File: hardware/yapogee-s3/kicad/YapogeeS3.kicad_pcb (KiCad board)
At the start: 2 copper layers, 0 parts

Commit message: pick bare s3 parts
Add the daughterboard BOM and checked local symbols and footprints for the bare ESP32-S3R8, high-side RFFC5072A converter, driver and power interfaces. Keep sourcing and review notes private; circuit capture and RF qualification remain.
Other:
- copper layers 2 -> 4
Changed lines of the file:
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@@
 	(title_block
 		(title "Yapogee S3")
-		(date "2026-10-27")
+		(date "2026-10-28")
 		(rev "Draft")
-		(comment 1 "Starter board - outline, stackup and routing not defined")
+		(comment 1 "Four-layer basis; outline, fabrication stackup and routing not defined")
 	)
 	(layers
 		(0 "F.Cu" signal)
+		(4 "In1.Cu" signal)
+		(6 "In2.Cu" signal)
 		(2 "B.Cu" signal)
 		(9 "F.Adhes" user "F.Adhesive")

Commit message: add standalone power and castellated interface
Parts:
- added J100: PCB edge interface, YapogeeS3_ModuleEdge_53x40_Castellated16_P2.00_EM3_v0.2, F.Cu at (100.0, 100.0)
- added J301: USB4105-GF-A-060, USB_C_Receptacle_GCT_USB4105_GF_A_16P, F.Cu at (103.7, 121.0)
- added J501: SMA-J-P-H-ST-EM3, Samtec_SMA_J_P_H_ST_EM3_DropInEdge, F.Cu at (100.0, 133.0)
- added SH1: BMI-S-206-F, KiCad_RF_Shielding_Laird_Technologies_BMI-S-206-F_36.83x33.68mm, F.Cu at (133.2, 120.0)
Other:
- board outline added: 53 x 40 mm
- board text added: "MECHANICAL DRAFT: 53 x 40 mm No circuit placement, nets or routing"

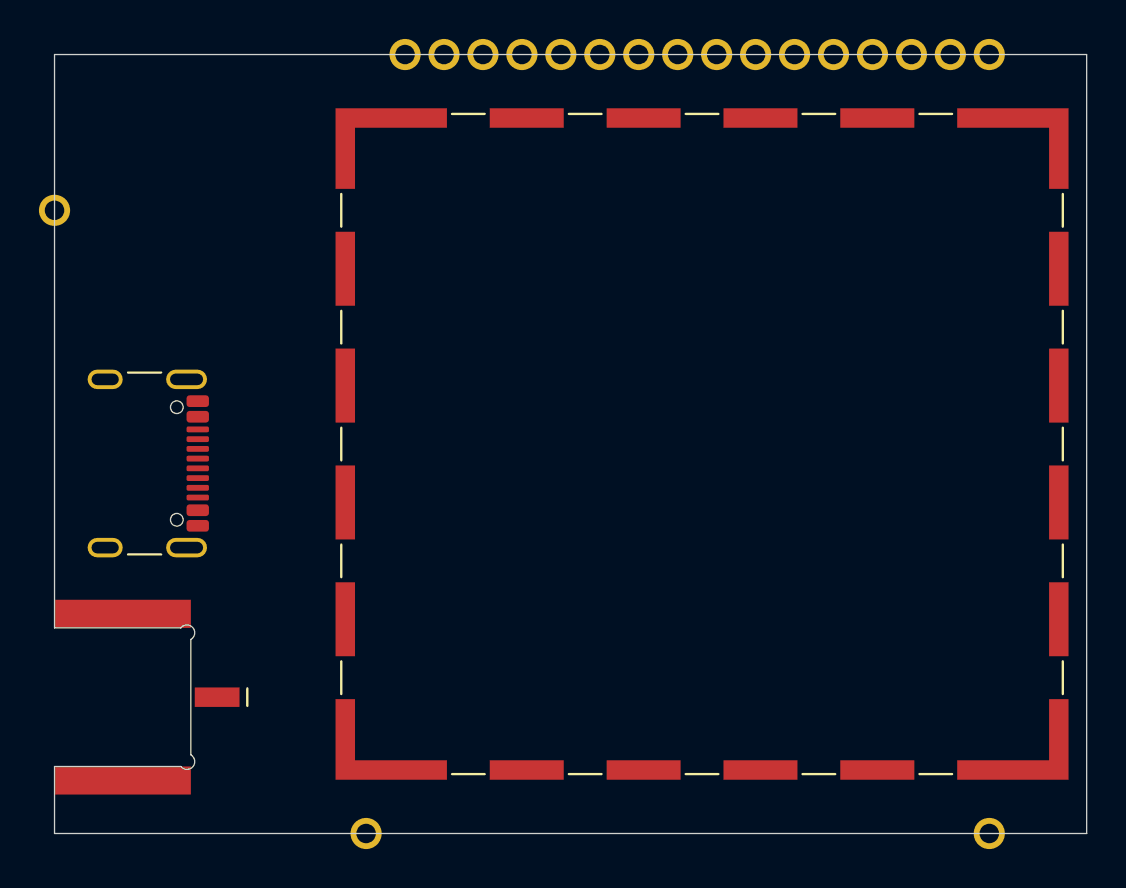
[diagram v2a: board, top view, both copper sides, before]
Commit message: adopt WROOM RF module and quiet 3V supply
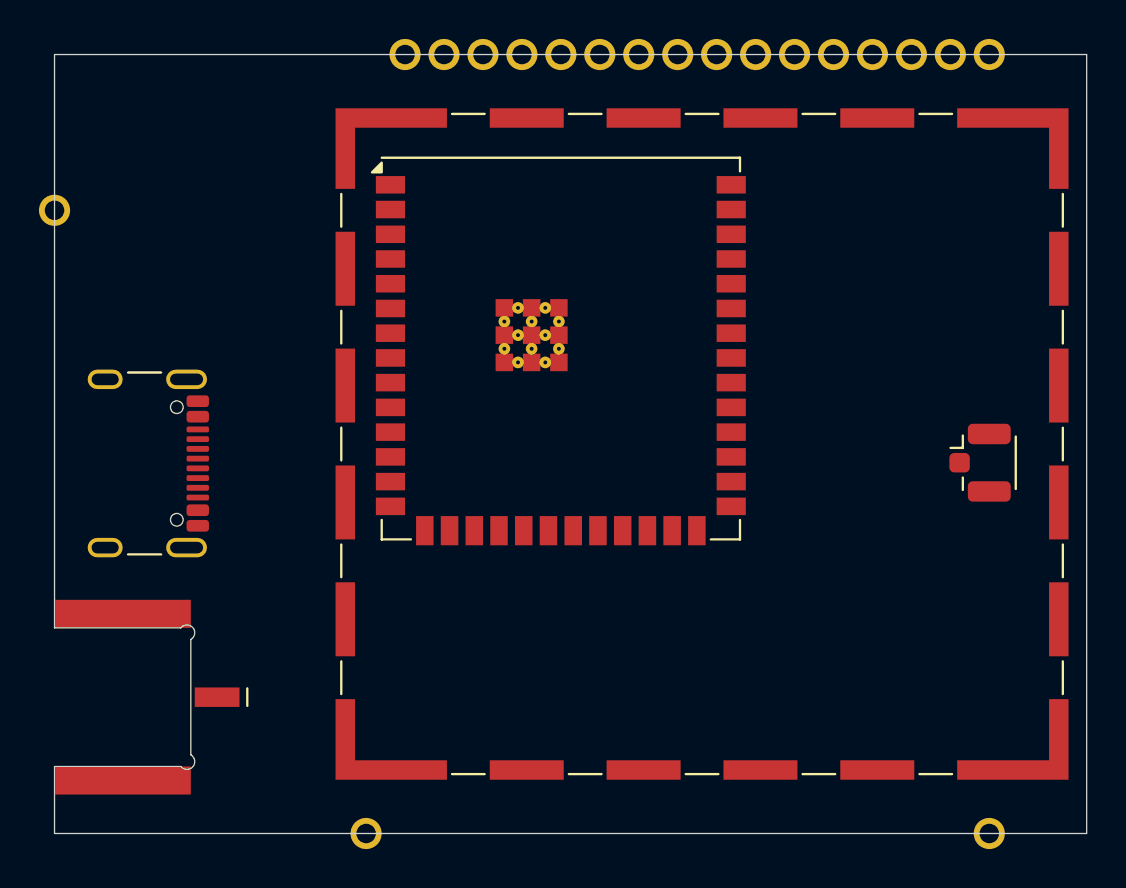
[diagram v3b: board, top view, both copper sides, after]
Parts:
- added J502: U.FL-R-SMT-1(80), Hirose_U_FL_R_SMT_1_80_HandSolder, F.Cu at (148.0, 121.0)
- added U101: ESP32-S3-WROOM-1U-N16R8, Espressif_ESP32_S3_WROOM_1U_18x19.2mm, F.Cu at (126.0, 115.1)
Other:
- board text added: "W501: 25 mm RF cable envelope Sample bend/height fit remains"
